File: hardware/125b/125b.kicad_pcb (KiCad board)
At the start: 2 copper layers, 59 x 75 mm, 48 parts, among them J1 Guitar in, J2 Barrel_Jack, J3 Conn_02x05_Odd_Even_MountingP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, J4 Guitar out, SW2 RotaryEncoder_Switch, SW3 SW_Push, SW4 SW_Push, U1 L78L05_TO92, U2 TL074

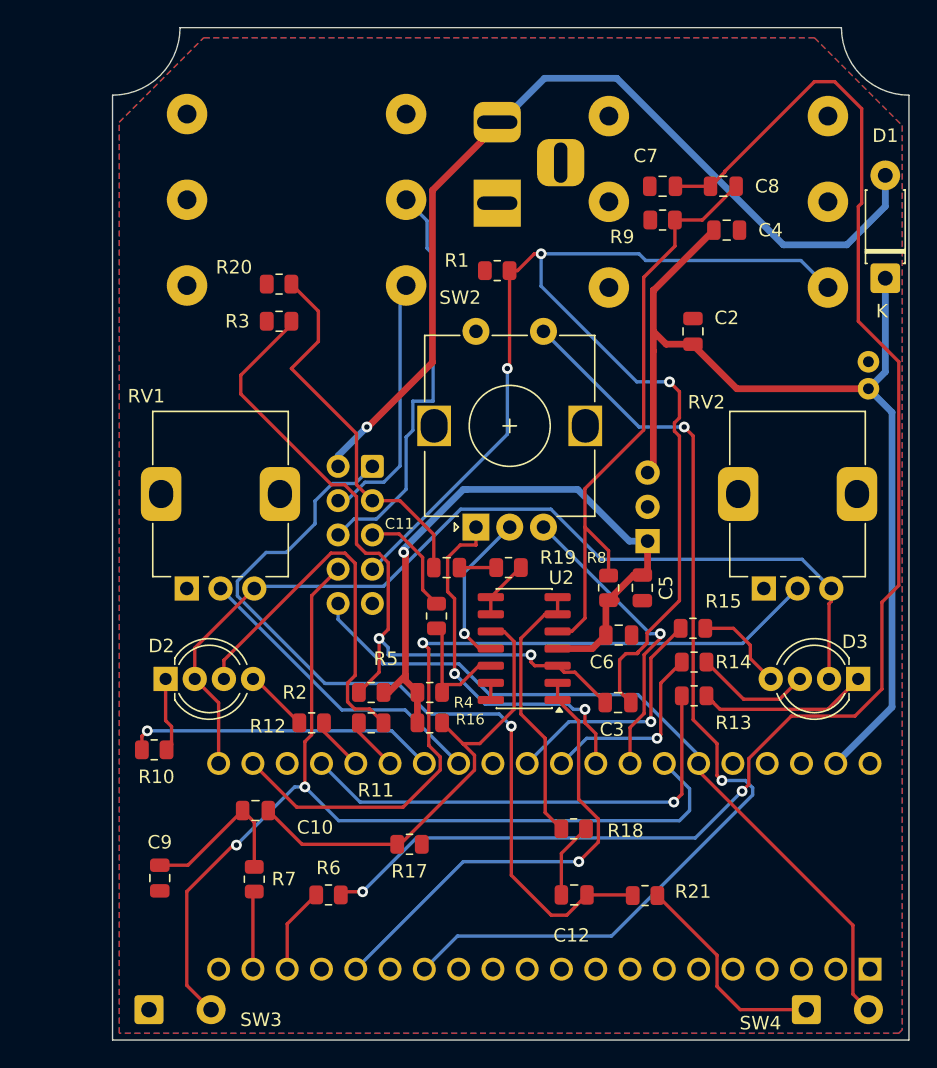
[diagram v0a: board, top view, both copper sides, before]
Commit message: Add stereo input to schematic and start pcb changes
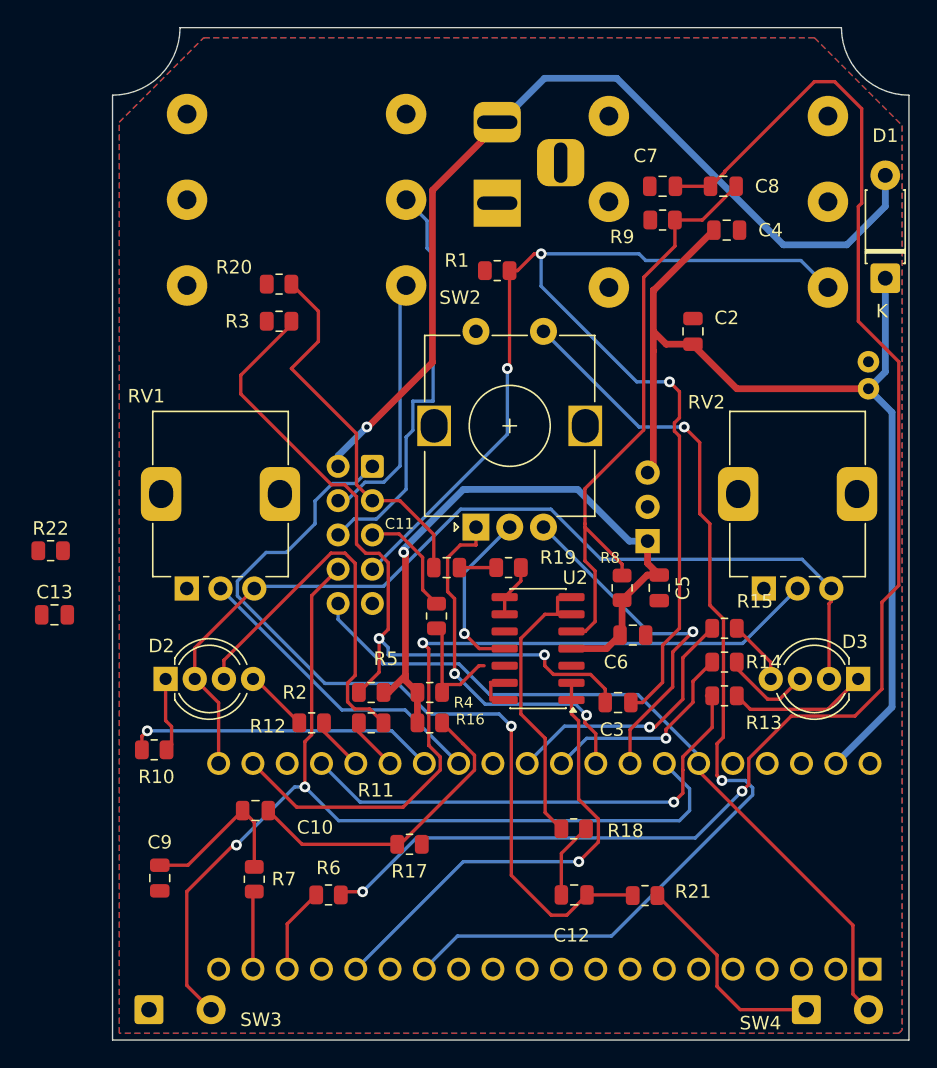
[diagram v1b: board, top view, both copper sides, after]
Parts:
- added C13: 1u, Capacitor_SMD:C_0805_2012Metric, F.Cu at (93.7, 78.5)
- added R22: 1M, Resistor_SMD:R_0805_2012Metric, F.Cu at (93.4, 73.8)
- moved R15 2.34 mm to (143.3, 79.5)
- moved R13 2.25 mm to (143.3, 84.5)
- moved R14 2.25 mm to (143.3, 82.0)
- moved C5 1.25 mm to (138.5, 76.5)
- moved C6 1.05 mm to (136.6, 80.0)
- moved U2 1.03 mm to (129.5, 81.0)
- moved R8 1.00 mm to (135.8, 76.5)
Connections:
- A1 pad 17: unconnected-(A1-AUDIO_IN_2-Pad17) -> /Right in
- J1 pad R: unconnected-(J1-PadR) -> /fsw9
- U2 pad 13: Net-(U2D--) -> /Right in
- U2 pad 14: Net-(U2D--) -> /Right in
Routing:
- net Net-(U2C-+): track 35.4 -> 23.1 mm
- net /ENC_B: track 22.5 -> 26.1 mm
- net Net-(D3-RK): track 13.3 -> 10.3 mm
- net Net-(D3-BK): track 6.98 -> 4.79 mm
- net Net-(D3-GK): track 8.68 -> 6.71 mm
- net /LED_2_R: track 35.4 -> 37.1 mm
- net /LED_2_B: track 18.3 -> 19.7 mm
- net Net-(U2D--): track 1.34 -> 0.00 mm
- net /Right in: track 0.00 -> 1.34 mm
- net /LED_2_G: track 14.3 -> 15.6 mm
- net Net-(U2C--): track 4.94 -> 3.99 mm
- net Net-(U2A-+): track 55.0 -> 55.7 mm
- net /fsw7: track 93.6 -> 92.9 mm
- net Net-(U2B-+): track 44.6 -> 45.2 mm
